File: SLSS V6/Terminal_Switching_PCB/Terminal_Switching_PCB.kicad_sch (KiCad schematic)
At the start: 4 parts, among them J1 +5V, J2 GND, J3 LED, J4 Solenoid

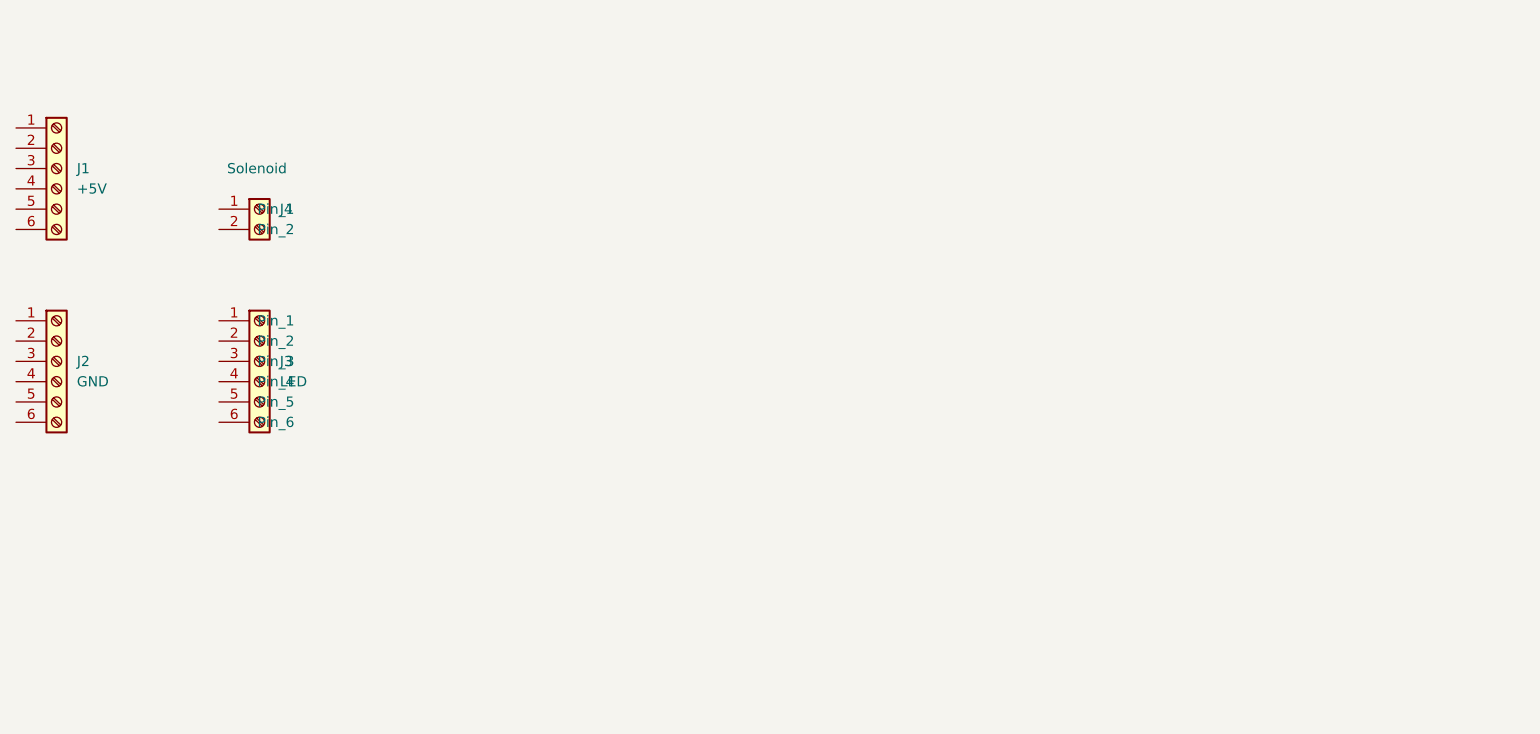
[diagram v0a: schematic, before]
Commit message: Created first PCB
needs placement adjustment
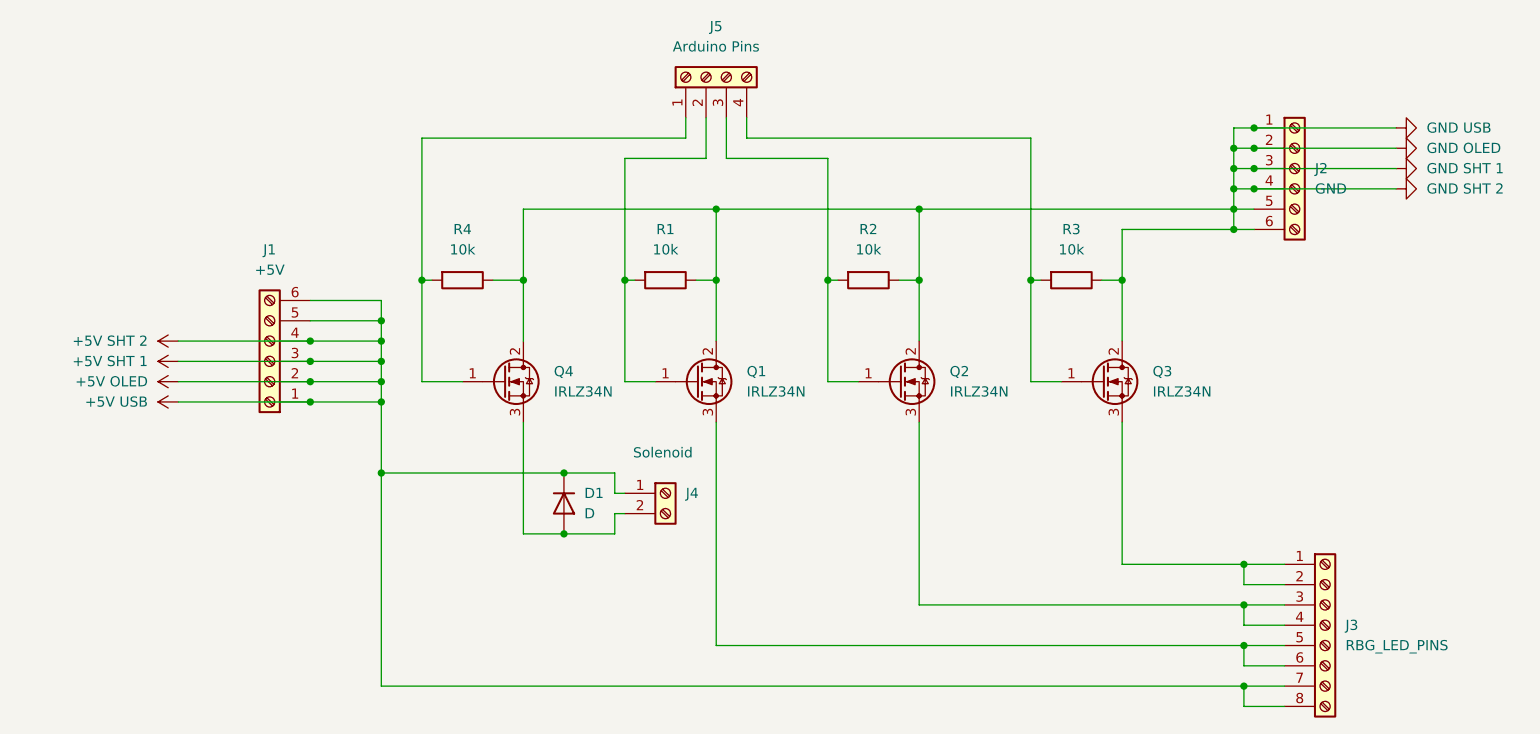
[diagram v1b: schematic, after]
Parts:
- removed J3: LED, TerminalBlock_Phoenix:TerminalBlock_Phoenix_MPT-0,5-6-2.54_1x06_P2.54mm_Horizontal, symbol Connector:Screw_Terminal_01x06
- added D1: D, Diode_THT:D_A-405_P10.16mm_Horizontal, symbol Device:D
- added J3: RBG_LED_PINS, TerminalBlock_Phoenix:TerminalBlock_Phoenix_MPT-0,5-8-2.54_1x08_P2.54mm_Horizontal, symbol Connector:Screw_Terminal_01x08
- added J5: Arduino Pins, TerminalBlock_Phoenix:TerminalBlock_Phoenix_MPT-0,5-4-2.54_1x04_P2.54mm_Horizontal, symbol Connector:Screw_Terminal_01x04
- added Q1, Q2, Q3, Q4: IRLZ34N, Package_TO_SOT_THT:TO-220-3_Vertical, symbol Transistor_FET:IRLZ34N
- added R1, R2, R3, R4: 10k, Resistor_THT:R_Axial_DIN0207_L6.3mm_D2.5mm_P10.16mm_Horizontal, symbol Device:R
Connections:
- net +5V OLED: now reaches J4.1 (Pin_1)
- net +5V OLED: now also J1.1 (Pin_1), J1.2 (Pin_2), J1.3 (Pin_3), J1.4 (Pin_4), J1.5 (Pin_5), J1.6 (Pin_6), D1.1 (K), J3.7 (Pin_7), J3.8 (Pin_8)
- net at J4.2 (Pin_2): now also D1.2 (A), Q4.3 (S)
- net GND OLED: now reaches J2.1 (Pin_1)
- net GND OLED: now also J2.2 (Pin_2), J2.3 (Pin_3), J2.4 (Pin_4), J2.5 (Pin_5), J2.6 (Pin_6), Q1.2 (D), Q2.2 (D), Q3.2 (D), Q4.2 (D), R1.1, R2.1, R3.1, R4.1
- new net: J5.1 (Pin_1), Q4.1 (G), R4.2
- new net: J3.1 (Pin_1), J3.2 (Pin_2), Q3.3 (S)
- new net: J3.3 (Pin_3), J3.4 (Pin_4), Q2.3 (S)
- new net: J3.5 (Pin_5), J3.6 (Pin_6), Q1.3 (S)
- new net: J5.2 (Pin_2), Q1.1 (G), R1.2
- new net: J5.3 (Pin_3), Q2.1 (G), R2.2
- new net: J5.4 (Pin_4), Q3.1 (G), R3.2
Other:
- moved on the sheet: J1, J2
